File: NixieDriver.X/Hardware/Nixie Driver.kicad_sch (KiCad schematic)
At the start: 20 parts, among them J1 Conn_02x03_Odd_Even, J2 Conn_01x03, J3 Conn_02x03_Odd_Even, Q0 MMBTA42LT1G, Q1 MMBTA42LT1G, Q10 MMBTA42LT1G, Q2 MMBTA42LT1G, Q3 MMBTA42LT1G, Q4 MMBTA42LT1G, Q5 MMBTA42LT1G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

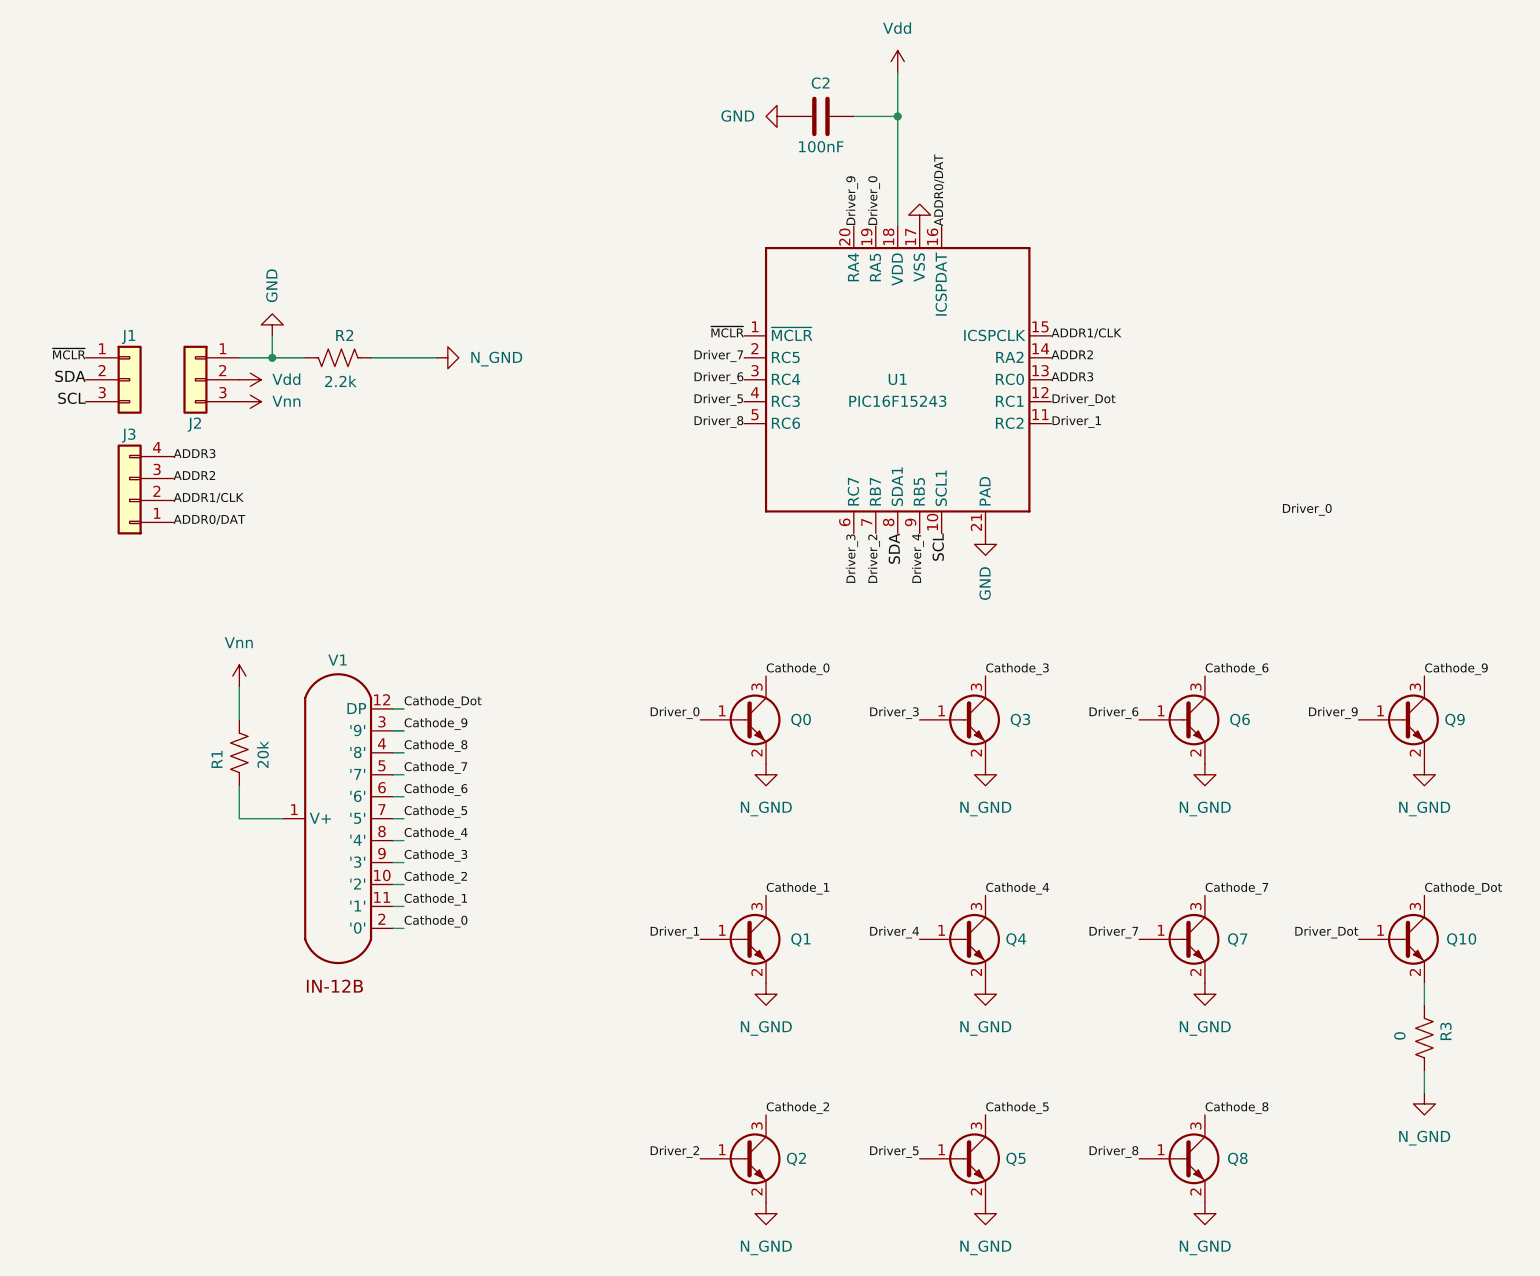
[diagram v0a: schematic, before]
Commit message: Current-limiting-resistor for each driver
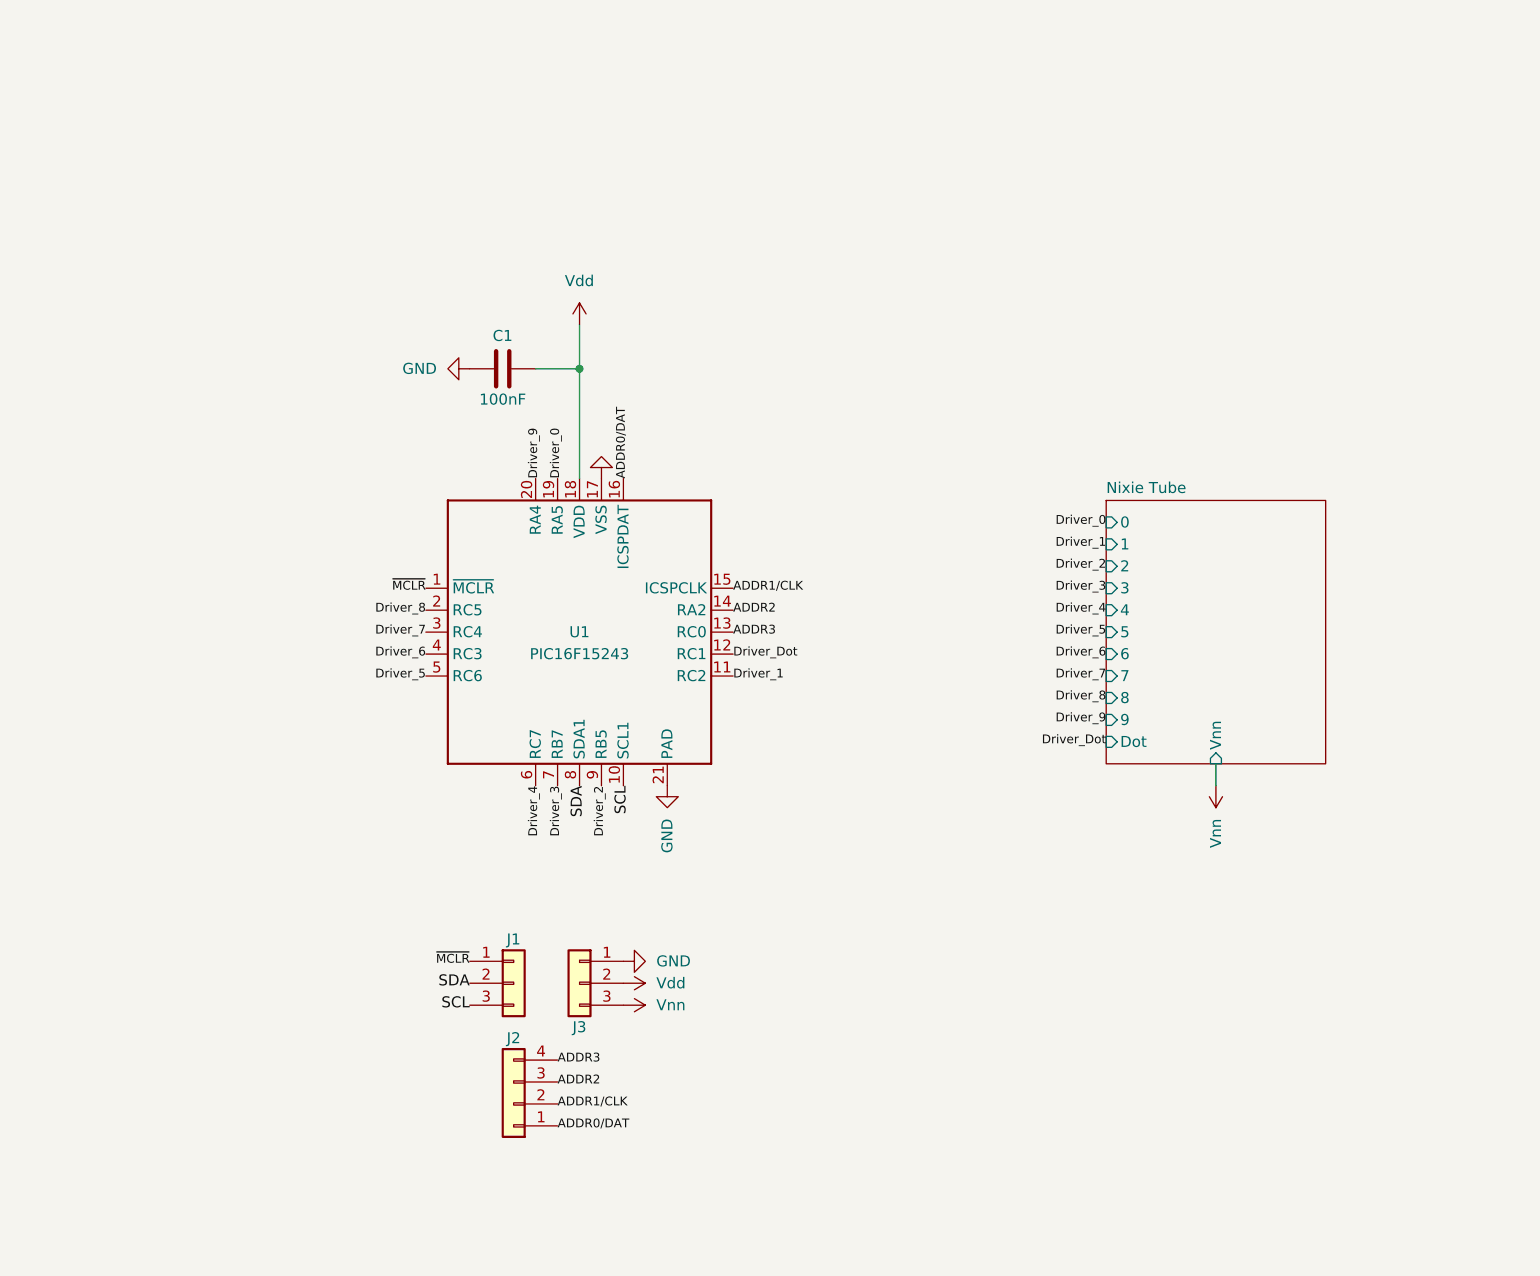
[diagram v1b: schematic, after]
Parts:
- removed Q0, Q1, Q10, Q2, Q3, Q4, Q5, Q6, Q7, Q8, Q9: MMBTA42LT1G, Package_TO_SOT_SMD:SOT-23, symbol Transistor_BJT:MMBTA42
- removed R1: 20k, Resistor_SMD:R_1206_3216Metric, symbol Device:R_US
- removed R2: 2.2k, Resistor_SMD:R_0805_2012Metric, symbol Device:R_US
- removed R3: 0, Resistor_SMD:R_0805_2012Metric, symbol Device:R_US
- removed V1: IN-12B, Nixie:IN-12[A_B] with center hole, symbol Nixie Driver-eagle-import:IN-12B
- renumbered C2 to C1, J3 to J2, J2 to J3
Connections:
- net Driver_2: now also U1.9 (RB5); no longer U1.7 (RB7)
- net Driver_3: now also U1.7 (RB7); no longer U1.6 (RC7)
- net Driver_4: now also U1.6 (RC7); no longer U1.9 (RB5)
- net Driver_5: now also U1.5 (RC6); no longer U1.4 (RC3)
- net Driver_6: now also U1.4 (RC3); no longer U1.3 (RC4)
- net Driver_7: now also U1.3 (RC4); no longer U1.2 (RC5)
- net Driver_8: now also U1.2 (RC5); no longer U1.5 (RC6)
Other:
- added sheet Nixie Tube (nixie-tube.kicad_sch)
- moved on the sheet: C1, J1, J2, J3, U1
